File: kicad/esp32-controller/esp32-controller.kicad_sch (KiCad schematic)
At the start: 28 parts, among them J1 Barrel_Jack_Switch, J2 RJ45, J3 RJ45, J4 RJ45, J5 RJ45, J6 Conn_01x04_Pin, U1 TPS560430, U2 SN65LVDS049, U3 SN65LVDS049, U4 ESP32-S3-WROOM-1

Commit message: Complete controller PCB v1
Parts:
- added R7: 10k, Resistor_SMD:R_0805_2012Metric, symbol Device:R
- added SW1, SW2: SW_Omron_B3FS, Button_Switch_SMD:SW_SPST_Omron_B3FS-100xP, symbol Switch:SW_Omron_B3FS
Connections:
- net +3V3: now also R7.1
- net GND: now also SW1.1, SW2.1
- net at C10.1, R6.2, U4.3 (EN): now also SW1.2
- net at U4.27 (IO0): now also R7.2, SW2.2
- net +5V renamed +12V
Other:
- moved on the sheet: C10, R6

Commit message: Cleanup
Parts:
- renumbered SW2 to BOOT1, SW1 to RESET1

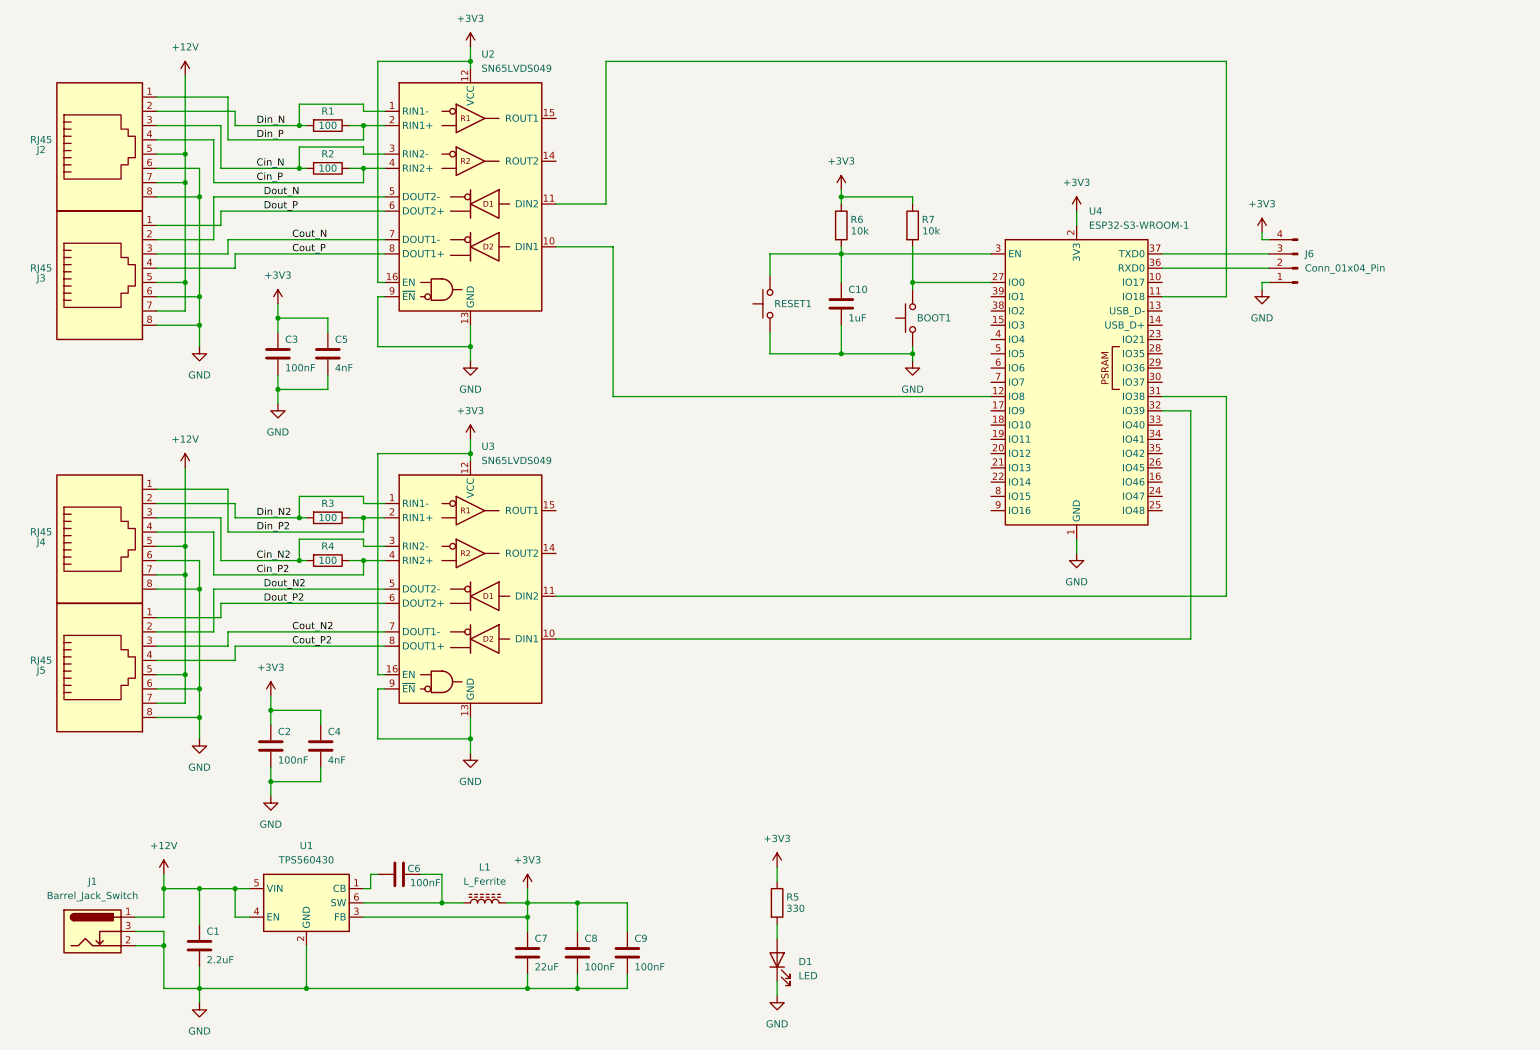
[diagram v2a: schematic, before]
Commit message: Migrate to 3 chain setup
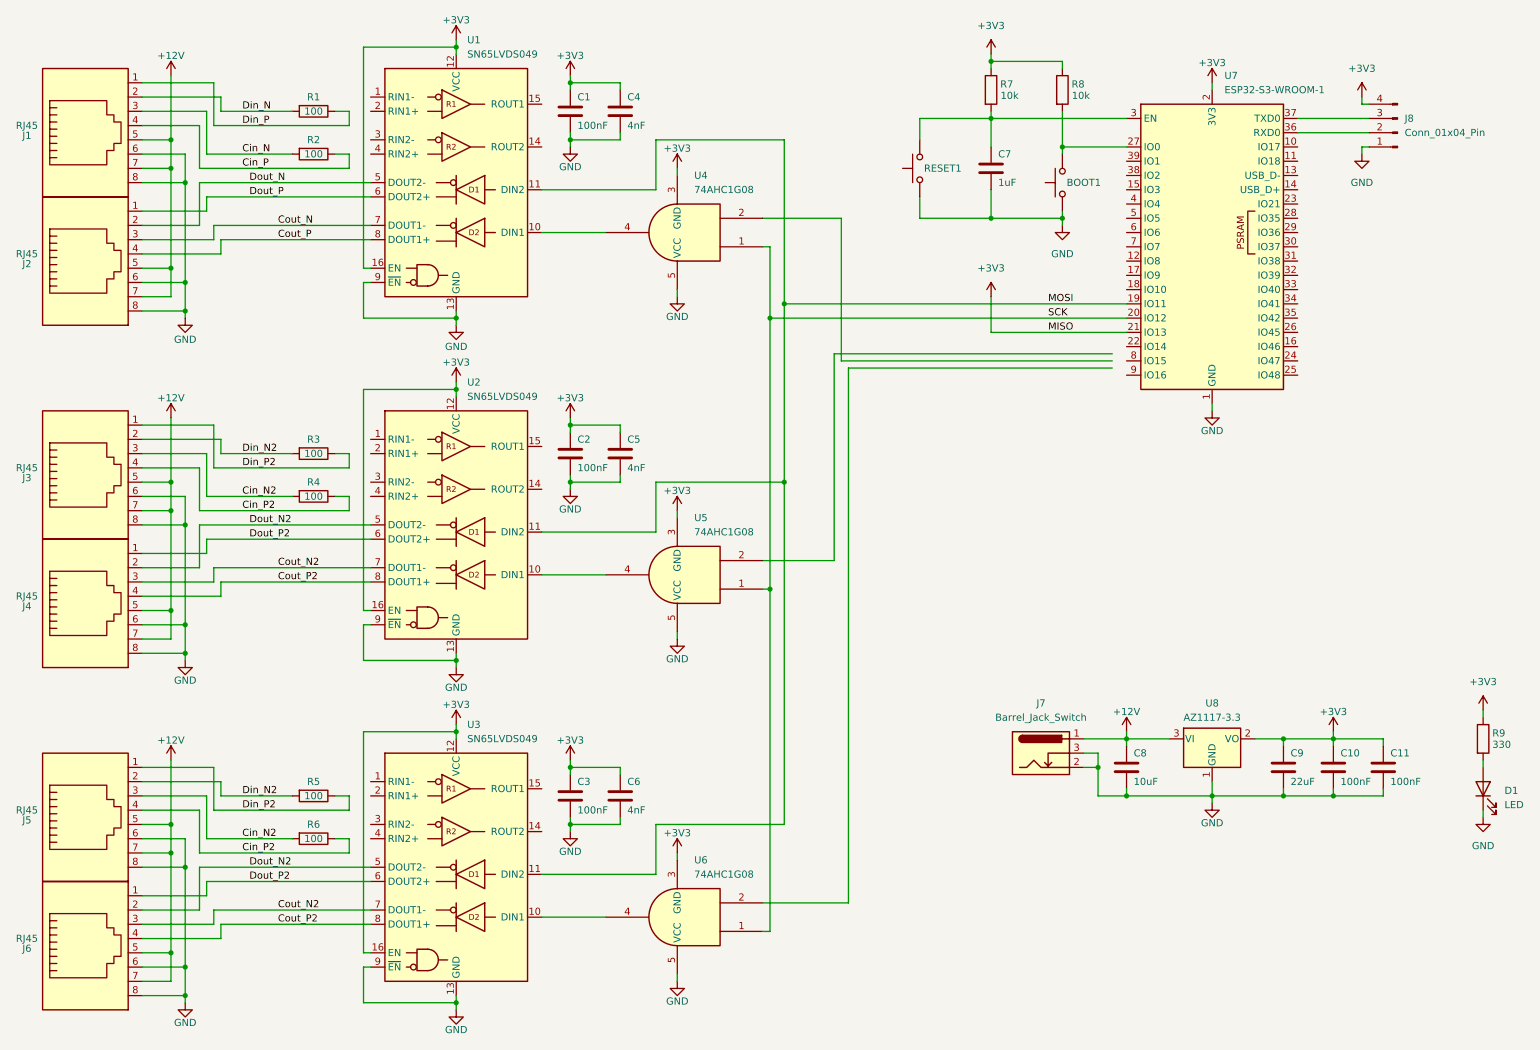
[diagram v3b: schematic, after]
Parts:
- removed C1: 2.2uF, Capacitor_SMD:C_0805_2012Metric, symbol Device:C
- removed C7: 22uF, Capacitor_SMD:C_0805_2012Metric, symbol Device:C
- removed J1: Barrel_Jack_Switch, Connector_BarrelJack:BarrelJack_Kycon_KLDX-0202-xC_Horizontal, symbol Connector:Barrel_Jack_Switch
- removed L1: L_Ferrite, Inductor_SMD:L_Bourns_SRP6060FA, symbol Device:L_Ferrite
- removed U1: TPS560430, Package_TO_SOT_SMD:SOT-23-6, symbol 042_my_lib:TPS560430
- added C10, C11, C3: 100nF, Capacitor_SMD:C_0805_2012Metric, symbol Device:C
- added J5, J6: RJ45, Connector_RJ:RJ45_Amphenol_54602-x08_Horizontal, symbol Connector:RJ45
- added J7: Barrel_Jack_Switch, Connector_BarrelJack:BarrelJack_Kycon_KLDX-0202-xC_Horizontal, symbol Connector:Barrel_Jack_Switch
- added R5, R6: 100, Resistor_SMD:R_0805_2012Metric, symbol Device:R
- added U3: SN65LVDS049, Package_SO:TSSOP-16_4.4x5mm_P0.65mm, symbol My_New_Library:SN65LVDS049
- added U4, U5, U6: 74AHC1G08, Package_TO_SOT_SMD:SOT-23-5_HandSoldering, symbol 74xGxx:74AHC1G08
- added U8: AZ1117-3.3, Package_TO_SOT_SMD:SOT-223-3_TabPin2, symbol Regulator_Linear:AZ1117-3.3
- C6: value 100nF -> 4nF
- C8: value 100nF -> 10uF
- C9: value 100nF -> 22uF
- renumbered C3 to C1, C5 to C4, C4 to C5, C10 to C7, J2 to J1, J3 to J2, J4 to J3, J5 to J4, J6 to J8, R6 to R7, R7 to R8, R5 to R9, U2 to U1, U3 to U2, U4 to U7
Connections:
- net +12V: now also C8.1, J5.5, J5.7, J6.5, J6.7, J7.1, U8.3 (VI)
- net +3V3: now also C6.1, U7.21 (IO13), C10.1, C11.1, C3.1, U3.12 (VCC), U3.16 (EN), U4.3 (GND), U5.3 (GND), U6.3 (GND), U8.2 (VO); no longer C8.1
- net Cin_N: no longer U1.3 (RIN2-)
- net Cin_N2: now also J5.3, R6.2; no longer U2.3 (RIN2-)
- net Cin_P: no longer U1.4 (RIN2+)
- net Cin_P2: now also J5.4, R6.1; no longer U2.4 (RIN2+)
- net Cout_N2: now also J6.3, U3.7 (DOUT1-)
- net Cout_P2: now also J6.4, U3.8 (DOUT1+)
- net Din_N: no longer U1.1 (RIN1-)
- net Din_N2: now also J5.2, R5.2; no longer U2.1 (RIN1-)
- net Din_P: no longer U1.2 (RIN1+)
- net Din_P2: now also J5.1, R5.1; no longer U2.2 (RIN1+)
- net Dout_N2: now also J6.2, U3.5 (DOUT2-)
- net Dout_P2: now also J6.1, U3.6 (DOUT2+)
- net GND: now also C6.2, C10.2, C11.2, C3.2, J5.6, J5.8, J6.6, J6.8, J7.2, J7.3, U3.13 (GND), U3.9 (~{EN}), U4.5 (VCC), U5.5 (VCC), U6.5 (VCC), U8.1 (GND)
- net at U1.10 (DIN1): now also U4.4; no longer U7.12 (IO8)
- net at U7.11 (IO18): no longer U1.11 (DIN2)
- net MOSI: now reaches U7.19 (IO11)
- net MOSI: now also U1.11 (DIN2), U2.11 (DIN2), U3.11 (DIN2)
- net SCK: now reaches U7.20 (IO12)
- net SCK: now also U4.1, U5.1, U6.1
- net at U7.31 (IO38): no longer U2.11 (DIN2)
- net at U7.32 (IO39): no longer U2.10 (DIN1)
- new net: U3.10 (DIN1), U6.4
- new net: U2.10 (DIN1), U5.4
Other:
- moved on the sheet: BOOT1, C1, C2, C4, C5, C7, D1, J1, J2, J3, J4, J8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
